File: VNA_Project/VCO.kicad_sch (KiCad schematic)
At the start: 16 parts, among them J1 Conn_Coaxial, Q1 BFR620

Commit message: Added ESP32 MCU design
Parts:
- renumbered C1 to C301, C2 to C302, C3 to C303, C5 to C304, C4 to C305, C7 to C306, C6 to C307, D1 to D301, J1 to J301, L1 to L301, L2 to L302, Q1 to Q301, R1 to R301, R3 to R302, R4 to R303, R2 to R304
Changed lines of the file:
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@@
 			(font
 				(size 3.81 3.81)
+				(thickness 0.762)
+				(bold yes)
+				(italic yes)
 			)
 		)
@@
 			(font
 				(size 3.81 3.81)
+				(thickness 0.762)
+				(bold yes)
+				(italic yes)
 			)
 		)
@@
 		(dnp no)
 		(fields_autoplaced yes)
-		(property "Reference" "C2"
+		(property "Reference" "C302"
 			(at 72.39 53.3401 0)
 			(effects
@@
 			(project "VNA_Project"
 				(path "/8b9c6944-c5f7-4a92-a452-dc4fa5f3924d/fea82b78-6456-42a4-9dbf-55f011a8ac47"
-					(reference "C2")
+					(reference "C302")
 					(unit 1)
 				)
@@
 		(dnp no)
 		(fields_autoplaced yes)
-		(property "Reference" "C5"
+		(property "Reference" "C304"
 			(at 104.14 82.5499 0)
 			(effects
@@
 			(project "VNA_Project"
 				(path "/8b9c6944-c5f7-4a92-a452-dc4fa5f3924d/fea82b78-6456-42a4-9dbf-55f011a8ac47"
-					(reference "C5")
+					(reference "C304")
 					(unit 1)
 				)
@@
 		(dnp no)
 		(fields_autoplaced yes)
-		(property "Reference" "J1"
+		(property "Reference" "J301"
 			(at 157.48 59.9831 0)
 			(effects
@@
 			(project ""
 				(path "/8b9c6944-c5f7-4a92-a452-dc4fa5f3924d/fea82b78-6456-42a4-9dbf-55f011a8ac47"
-					(reference "J1")
+					(reference "J301")
 					(unit 1)
 				)
@@
 		(dnp no)
 		(fields_autoplaced yes)
-		(property "Reference" "R1"
+		(property "Reference" "R301"
 			(at 34.29 71.1199 0)
 			(effects
@@
 			(project ""
 				(path "/8b9c6944-c5f7-4a92-a452-dc4fa5f3924d/fea82b78-6456-42a4-9dbf-55f011a8ac47"
-					(reference "R1")
+					(reference "R301")
 					(unit 1)
 				)
@@
 		(dnp no)
 		(fields_autoplaced yes)
-		(property "Reference" "C1"
+		(property "Reference" "C301"
 			(at 55.88 71.1199 0)
 			(effects
@@
 			(project ""
 				(path "/8b9c6944-c5f7-4a92-a452-dc4fa5f3924d/fea82b78-6456-42a4-9dbf-55f011a8ac47"
-					(reference "C1")
+					(reference "C301")
 					(unit 1)
 				)
@@
 		(dnp no)
 		(fields_autoplaced yes)
-		(property "Reference" "C4"
+		(property "Reference" "C305"
 			(at 134.62 72.39 90)
 			(effects
@@
 			(project "VNA_Project"
 				(path "/8b9c6944-c5f7-4a92-a452-dc4fa5f3924d/fea82b78-6456-42a4-9dbf-55f011a8ac47"
-					(reference "C4")
+					(reference "C305")
 					(unit 1)
 				)
@@
 		(dnp no)
 		(fields_autoplaced yes)
-		(property "Reference" "#PWR06"
+		(property "Reference" "#PWR0304"
 			(at 100.33 97.79 0)
 			(effects
@@
 			(project "VNA_Project"
 				(path "/8b9c6944-c5f7-4a92-a452-dc4fa5f3924d/fea82b78-6456-42a4-9dbf-55f011a8ac47"
-					(reference "#PWR06")
+					(reference "#PWR0304")
 					(unit 1)
 				)
@@
 		(dnp no)
 		(fields_autoplaced yes)
-		(property "Reference" "#PWR05"
+		(property "Reference" "#PWR0307"
 			(at 138.43 90.17 0)
 			(effects
@@
 			(project "VNA_Project"
 				(path "/8b9c6944-c5f7-4a92-a452-dc4fa5f3924d/fea82b78-6456-42a4-9dbf-55f011a8ac47"
-					(reference "#PWR05")
+					(reference "#PWR0307")
 					(unit 1)
 				)
@@
 		(dnp no)
 		(fields_autoplaced yes)
-		(property "Reference" "L1"
+		(property "Reference" "L301"
 			(at 59.69 55.88 90)
 			(effects
@@
 			(project ""
 				(path "/8b9c6944-c5f7-4a92-a452-dc4fa5f3924d/fea82b78-6456-42a4-9dbf-55f011a8ac47"
-					(reference "L1")
+					(reference "L301")
 					(unit 1)
 				)
@@
 		(dnp no)
 		(fields_autoplaced yes)
-		(property "Reference" "#PWR04"
+		(property "Reference" "#PWR0306"
 			(at 127 101.6 0)
 			(effects
@@
 			(project "VNA_Project"
 				(path "/8b9c6944-c5f7-4a92-a452-dc4fa5f3924d/fea82b78-6456-42a4-9dbf-55f011a8ac47"
-					(reference "#PWR04")
+					(reference "#PWR0306")
 					(unit 1)
 				)
@@
 		(dnp no)
 		(fields_autoplaced yes)
-		(property "Reference" "L2"
+		(property "Reference" "L302"
 			(at 128.27 48.2599 0)
 			(effects
@@
 			(project ""
 				(path "/8b9c6944-c5f7-4a92-a452-dc4fa5f3924d/fea82b78-6456-42a4-9dbf-55f011a8ac47"
-					(reference "L2")
+					(reference "L302")
 					(unit 1)
 				)
@@
 		(dnp no)
 		(fields_autoplaced yes)
-		(property "Reference" "#PWR09"
+		(property "Reference" "#PWR0309"
 			(at 153.67 76.2 0)
 			(effects
@@
 			(project "VNA_Project"
 				(path "/8b9c6944-c5f7-4a92-a452-dc4fa5f3924d/fea82b78-6456-42a4-9dbf-55f011a8ac47"
-					(reference "#PWR09")
+					(reference "#PWR0309")
 					(unit 1)
 				)
@@
 		(dnp no)
 		(fields_autoplaced yes)
-		(property "Reference" "D1"
+		(property "Reference" "D301"
 			(at 54.61 81.2799 90)
 			(effects
@@
 			(project ""
 				(path "/8b9c6944-c5f7-4a92-a452-dc4fa5f3924d/fea82b78-6456-42a4-9dbf-55f011a8ac47"
-					(reference "D1")
+					(reference "D301")
 					(unit 1)
 				)
@@
 		(dnp no)
 		(fields_autoplaced yes)
-		(property "Reference" "R3"
+		(property "Reference" "R302"
 			(at 102.87 49.5299 0)
 			(effects
@@
 			(project ""
 				(path "/8b9c6944-c5f7-4a92-a452-dc4fa5f3924d/fea82b78-6456-42a4-9dbf-55f011a8ac47"
-					(reference "R3")
+					(reference "R302")
 					(unit 1)
 				)
@@
 		(dnp no)
 		(fields_autoplaced yes)
-		(property "Reference" "Q1"
+		(property "Reference" "Q301"
 			(at 129.54 66.0399 0)
 			(effects
@@
 			(project ""
 				(path "/8b9c6944-c5f7-4a92-a452-dc4fa5f3924d/fea82b78-6456-42a4-9dbf-55f011a8ac47"
-					(reference "Q1")
+					(reference "Q301")
 					(unit 1)
 				)
@@
 		(dnp no)
 		(fields_autoplaced yes)
-		(property "Reference" "#PWR03"
+		(property "Reference" "#PWR0303"
 			(at 76.2 40.64 0)
 			(effects
@@
 			(project "VNA_Project"
 				(path "/8b9c6944-c5f7-4a92-a452-dc4fa5f3924d/fea82b78-6456-42a4-9dbf-55f011a8ac47"
-					(reference "#PWR03")
+					(reference "#PWR0303")
 					(unit 1)
 				)
@@
 		(on_board yes)
 		(dnp no)
-		(property "Reference" "C3"
+		(property "Reference" "C303"
 			(at 86.36 70.358 90)
 			(effects
@@
 			(project "VNA_Project"
 				(path "/8b9c6944-c5f7-4a92-a452-dc4fa5f3924d/fea82b78-6456-42a4-9dbf-55f011a8ac47"
-					(reference "C3")
+					(reference "C303")
 					(unit 1)
 				)
@@
 		(dnp no)
 		(fields_autoplaced yes)
-		(property "Reference" "#PWR07"
+		(property "Reference" "#PWR0305"
 			(at 127 34.29 0)
 			(effects
@@
 			(project ""
 				(path "/8b9c6944-c5f7-4a92-a452-dc4fa5f3924d/fea82b78-6456-42a4-9dbf-55f011a8ac47"
-					(reference "#PWR07")
+					(reference "#PWR0305")
 					(unit 1)
 				)
@@
 		(dnp no)
 		(fields_autoplaced yes)
-		(property "Reference" "C6"
+		(property "Reference" "C307"
 			(at 138.43 35.56 90)
 			(effects
@@
 			(project "VNA_Project"
 				(path "/8b9c6944-c5f7-4a92-a452-dc4fa5f3924d/fea82b78-6456-42a4-9dbf-55f011a8ac47"
-					(reference "C6")
+					(reference "C307")
 					(unit 1)
 				)
@@
 		(dnp no)
 		(fields_autoplaced yes)
-		(property "Reference" "R2"
+		(property "Reference" "R304"
 			(at 129.54 87.6299 0)
 			(effects
@@
 			(project ""
 				(path "/8b9c6944-c5f7-4a92-a452-dc4fa5f3924d/fea82b78-6456-42a4-9dbf-55f011a8ac47"
-					(reference "R2")
+					(reference "R304")
 					(unit 1)
 				)
@@
 		(dnp no)
 		(fields_autoplaced yes)
-		(property "Reference" "C7"
+		(property "Reference" "C306"
 			(at 137.16 53.34 90)
 			(effects
@@
 			(project "VNA_Project"
 				(path "/8b9c6944-c5f7-4a92-a452-dc4fa5f3924d/fea82b78-6456-42a4-9dbf-55f011a8ac47"
-					(reference "C7")
+					(reference "C306")
 					(unit 1)
 				)
@@
 		(dnp no)
 		(fields_autoplaced yes)
-		(property "Reference" "#PWR01"
+		(property "Reference" "#PWR0301"
 			(at 31.75 69.85 0)
 			(effects
@@
 			(project ""
 				(path "/8b9c6944-c5f7-4a92-a452-dc4fa5f3924d/fea82b78-6456-42a4-9dbf-55f011a8ac47"
-					(reference "#PWR01")
+					(reference "#PWR0301")
 					(unit 1)
 				)
@@
 		(dnp no)
 		(fields_autoplaced yes)
-		(property "Reference" "#PWR02"
+		(property "Reference" "#PWR0302"
 			(at 52.07 96.52 0)
 			(effects
@@
 			(project ""
 				(path "/8b9c6944-c5f7-4a92-a452-dc4fa5f3924d/fea82b78-6456-42a4-9dbf-55f011a8ac47"
-					(reference "#PWR02")
+					(reference "#PWR0302")
 					(unit 1)
 				)
@@
 		(dnp no)
 		(fields_autoplaced yes)
-		(property "Reference" "R4"
+		(property "Reference" "R303"
 			(at 129.54 35.5599 0)
 			(effects
@@
 			(project "VNA_Project"
 				(path "/8b9c6944-c5f7-4a92-a452-dc4fa5f3924d/fea82b78-6456-42a4-9dbf-55f011a8ac47"
-					(reference "R4")
+					(reference "R303")
 					(unit 1)
 				)
@@
 		(dnp no)
 		(fields_autoplaced yes)
-		(property "Reference" "#PWR08"
+		(property "Reference" "#PWR0308"
 			(at 142.24 52.07 0)
 			(effects
@@
 			(project "VNA_Project"
 				(path "/8b9c6944-c5f7-4a92-a452-dc4fa5f3924d/fea82b78-6456-42a4-9dbf-55f011a8ac47"
-					(reference "#PWR08")
-					(unit 1)
-				)
+					(reference "#PWR0308")
+					(unit 1)
+				)

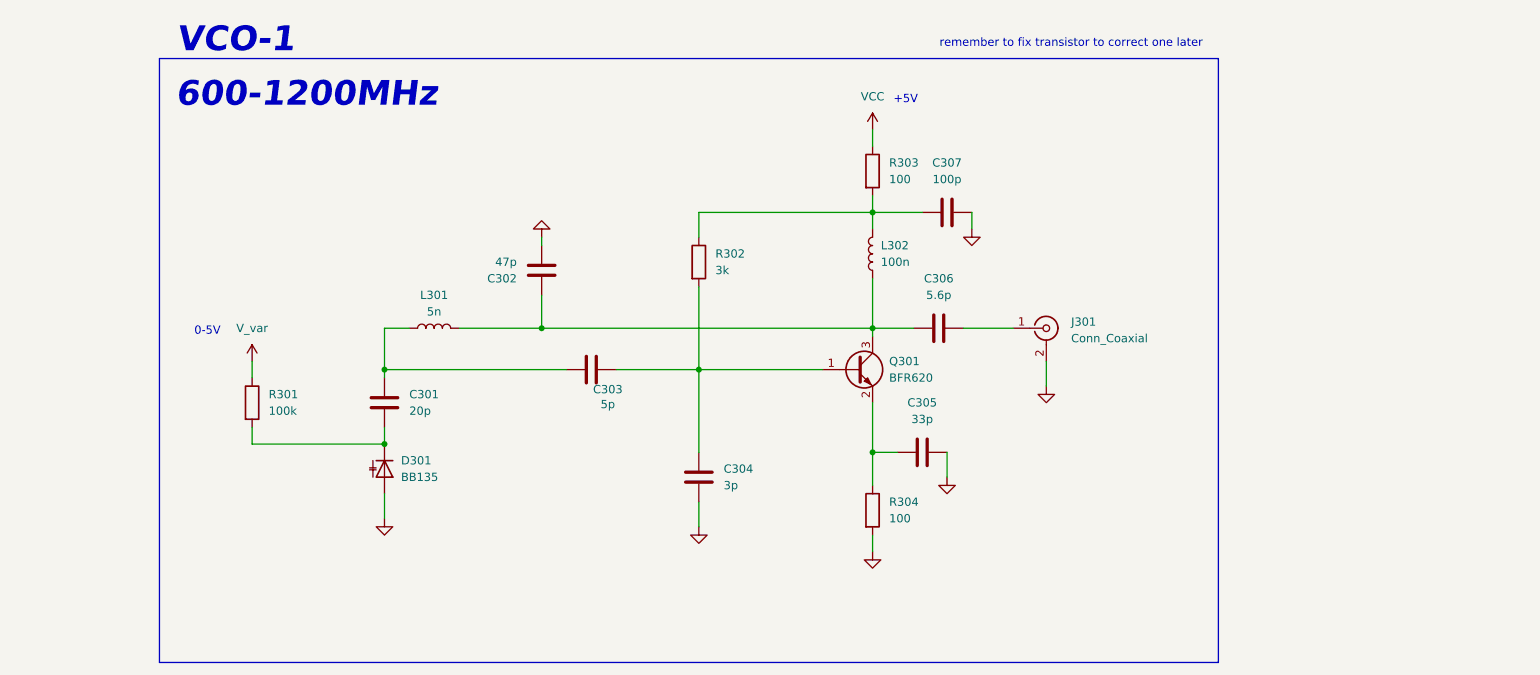
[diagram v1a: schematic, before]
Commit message: finishing up front end
refining Non RF front end
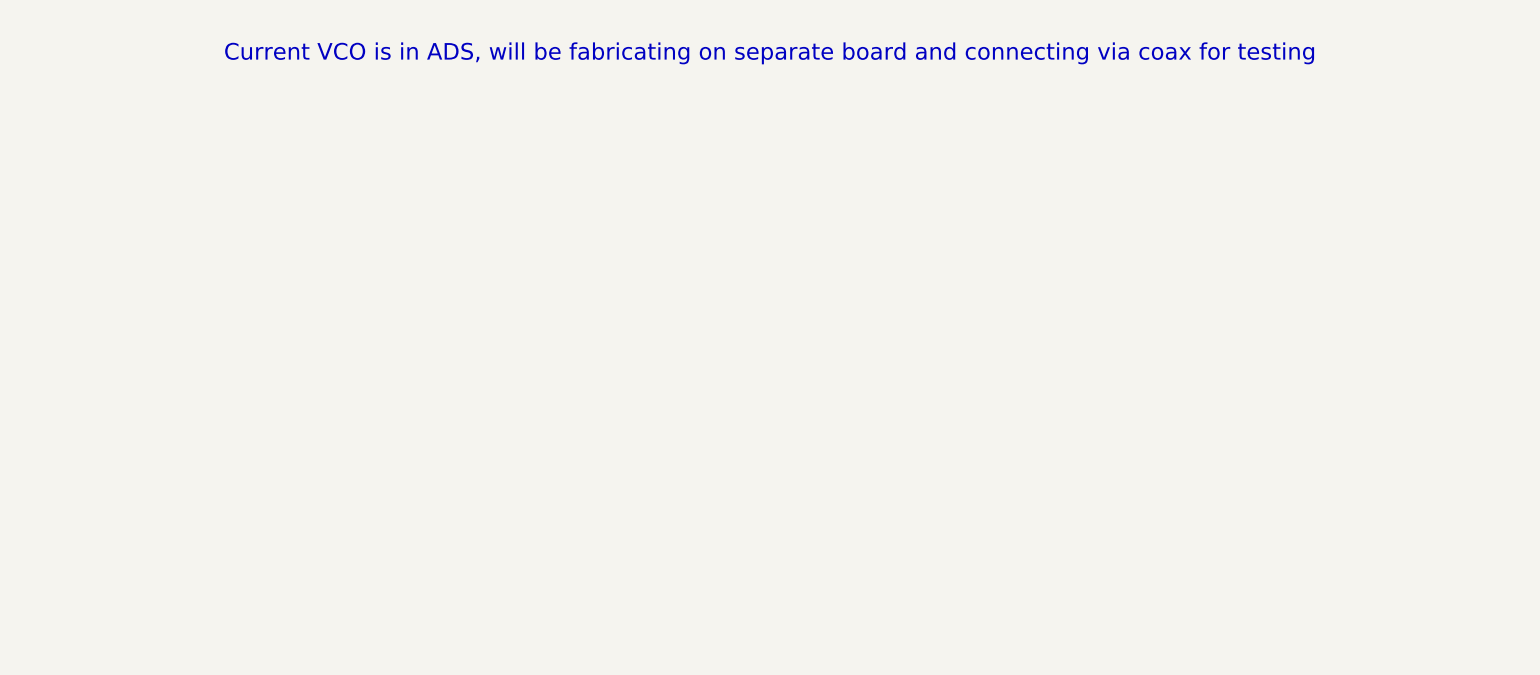
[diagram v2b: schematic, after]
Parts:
- removed C301: 20p, symbol Device:C
- removed C302: 47p, symbol Device:C
- removed C303: 5p, symbol Device:C
- removed C304: 3p, symbol Device:C
- removed C305: 33p, symbol Device:C
- removed C306: 5.6p, symbol Device:C
- removed C307: 100p, symbol Device:C
- removed D301: BB135, symbol Device:D_Capacitance
- removed J301: Conn_Coaxial, symbol Connector:Conn_Coaxial
- removed L301: 5n, symbol Device:L
- removed L302: 100n, symbol Device:L
- removed Q301: BFR620, Package_TO_SOT_SMD:SOT-323_SC-70, symbol Transistor_BJT:BFR92
- removed R301: 100k, symbol Device:R
- removed R302: 3k, symbol Device:R
- removed R303, R304: 100, symbol Device:R
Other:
- note added: "Current VCO is in ADS, will be fabricating on separate board and connecting via coax for testing"
- note removed: "+5V"
- note removed: "0-5V"
- note removed: "600-1200MHz"
- note removed: "VCO-1"
- note removed: "remember to fix transistor to correct one later"
